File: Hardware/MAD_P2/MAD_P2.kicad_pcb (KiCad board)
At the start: 4 copper layers, 132.1 x 145.5 mm, 305 parts, among them J1 Line_3, J10 Conn_02x05_Odd_Even, J11 Conn_02x05_Odd_Even, J12 Micro_SD_Card, J13 Conn_02x05_Odd_Even, J14 Conn_02x05_Odd_Even, J15 Conn_ADC1, J16 Conn_DAC, J17 Conn_ADC2, J18 P3, J19 P4, J2 Line_1, J20 P2, J21 Conn_02x05_Odd_Even, J22 Conn_02x05_Odd_Even, J23 Conn_02x03_Odd_Even, J24 P5, J25 P6, J26 P7, J3 Line_2, J4 Power_In, J5 Micro_SD_Card, J6 Edge_Conn, J7 Conn_02x05_Odd_Even, J8 USB_C_Receptacle_USB2.0, J9 Conn_02x05_Odd_Even, P10 CONN_01X01, P11 CONN_01X01, P13 CONN_01X01, P8 CONN_01X01, Q1 MMBT3904, U1 P2X8C4M64P-REF, U10 AMS1117-3.3, U11 APM4953, U12 APM4953, U13 XL1509-5.0, U14 XL1509-5.0, U15 AMS1117-3.3, U16 AMS1117-3.3, U17 AMS1117-3.3, U18 AMS1117-3.3, U19 AMS1117-1.8, U2 XL1509-5.0, U20 LM321, U21 APM4953, U22 XL1509-5.0, U23 AMS1117-3.3, U24 AMS1117-3.3, U25 AMS1117-1.8, U26 W25Q128JVS, U27 FT232RL, U28 DS3231M, U29 ESP-12F, U3 XL1509-5.0, U30 ADS131E08-REF, U31 MAX5134-7, U4 XL1509-5.0, U5 XL1509-5.0, U6 AMS1117-3.3, U7 AMS1117-3.3, U8 AMS1117-3.3, U9 AMS1117-3.3, Y1 20MHz

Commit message: revising pcb layout
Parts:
- removed C132, C133, C134: 470pF, Capacitor_SMD:C_0603_1608Metric
- removed C135: 47pF, Capacitor_SMD:C_0603_1608Metric
- removed C136, C138: 0.1uF, Capacitor_SMD:C_0603_1608Metric
- removed C137, C139: 4.7uF, Capacitor_SMD:C_0603_1608Metric
- removed TP14: ADC_AMPP, TestPoint:TestPoint_Pad_1.0x1.0mm
- removed TP15: ADC_AMPN, TestPoint:TestPoint_Pad_1.0x1.0mm
- removed TP16: ADC_AMPOUT, TestPoint:TestPoint_Pad_1.0x1.0mm
- removed U25: AMS1117-1.8, Package_TO_SOT_SMD:SOT-223-3_TabPin2
- removed U30: ADS131E08-REF, Package_QFP:TQFP-64_10x10mm_P0.5mm
- removed U31: MAX5134-7, Package_SO:TSSOP-16_4.4x5mm_P0.65mm
- added D13: BLUE, LED_SMD:LED_0603_1608Metric, F.Cu at (324.0, 62.8)
- added D14: BLUE, LED_SMD:LED_0603_1608Metric, F.Cu at (314.7, 69.9)
- added D15: BLUE, LED_SMD:LED_0603_1608Metric, F.Cu at (357.2, 29.0)
- added D16: BLUE, LED_SMD:LED_0603_1608Metric, F.Cu at (357.2, 31.6)
- added D17: BLUE, LED_SMD:LED_0603_1608Metric, F.Cu at (318.7, 69.9)
- added D18: BLUE, LED_SMD:LED_0603_1608Metric, F.Cu at (341.9, 49.5)
- added D19: BLUE, LED_SMD:LED_0603_1608Metric, F.Cu at (328.0, 62.8)
- added D20: BLUE, LED_SMD:LED_0603_1608Metric, F.Cu at (324.0, 68.0)
- added D21: BLUE, LED_SMD:LED_0603_1608Metric, F.Cu at (324.0, 65.4)
- added D22: BLUE, LED_SMD:LED_0603_1608Metric, F.Cu at (346.2, 45.9)
- added D5: BLUE, LED_SMD:LED_0603_1608Metric, F.Cu at (357.2, 34.2)
- added D7: BLUE, LED_SMD:LED_0603_1608Metric, F.Cu at (306.6, 69.9)
- added D8: BLUE, LED_SMD:LED_0603_1608Metric, F.Cu at (310.6, 69.9)
- added F1: 5A, Fuse:Fuse_1206_3216Metric, F.Cu at (402.4, 19.9)
- added F2: 5A, Fuse:Fuse_1206_3216Metric, F.Cu at (410.8, 19.7)
- added F3: 5A, Fuse:Fuse_1206_3216Metric, F.Cu at (413.3, 19.8)
- added F5: 5A, Fuse:Fuse_1206_3216Metric, F.Cu at (421.7, 19.9)
- added J27: Line_1_1, MAD_P2:0705530001, B.Cu at (418.6, 27.3)
- added J28: Line_2_1, MAD_P2:0705530001, B.Cu at (445.4, 27.3)
- added J29: Line_2_3, MAD_P2:0705530001, B.Cu at (463.3, 27.3)
- added J30: Line_3_2, MAD_P2:0705530001, B.Cu at (481.2, 27.3)
- added J31: Micro_SD_Card_Connector, Tensile_Board:WM26501, F.Cu at (372.0, 30.8)
- added J32: Micro_SD_Card_Socket, Connector_Card:microSD_HC_Hirose_DM3D-SF, B.Cu at (372.0, 38.5)
- added J33: Shifted IO, Connector_PinSocket_2.54mm:PinSocket_1x06_P2.54mm_Vertical, F.Cu at (280.7, 78.5)
- added JP11: Jumper_1_3.3V, Jumper:SolderJumper-2_P1.3mm_Open_Pad1.0x1.5mm, F.Cu at (342.0, 46.4)
- added JP12: Jumper_1_5V, Jumper:SolderJumper-2_P1.3mm_Open_Pad1.0x1.5mm, F.Cu at (302.3, 70.4)
- added JP22: Jumper_1_3.3V, Jumper:SolderJumper-2_P1.3mm_Open_Pad1.0x1.5mm, F.Cu at (284.9, 70.4)
- added JP23: Jumper_1_5V, Jumper:SolderJumper-2_P1.3mm_Open_Pad1.0x1.5mm, F.Cu at (280.6, 66.8)
- added JP24: Jumper_1_VIN, Jumper:SolderJumper-2_P1.3mm_Open_Pad1.0x1.5mm, F.Cu at (302.3, 66.8)
- added JP25: Jumper_2_3.3V, Jumper:SolderJumper-2_P1.3mm_Open_Pad1.0x1.5mm, F.Cu at (306.7, 63.3)
- added JP26: Jumper_2_5V, Jumper:SolderJumper-2_P1.3mm_Open_Pad1.0x1.5mm, F.Cu at (302.3, 63.3)
- added JP27: Jumper_2_VIN, Jumper:SolderJumper-2_P1.3mm_Open_Pad1.0x1.5mm, F.Cu at (284.9, 63.3)
- added JP28: Jumper_2_3.3V, Jumper:SolderJumper-2_P1.3mm_Open_Pad1.0x1.5mm, F.Cu at (280.6, 63.3)
- added JP29: Jumper_2_5V, Jumper:SolderJumper-2_P1.3mm_Open_Pad1.0x1.5mm, F.Cu at (289.3, 63.3)
- added JP30: Jumper_2_VIN, Jumper:SolderJumper-2_P1.3mm_Open_Pad1.0x1.5mm, F.Cu at (293.6, 63.3)
- added JP31: Jumper_3_3.3V, Jumper:SolderJumper-2_P1.3mm_Open_Pad1.0x1.5mm, F.Cu at (289.3, 66.8)
- added JP32: Jumper_3_5V, Jumper:SolderJumper-2_P1.3mm_Open_Pad1.0x1.5mm, F.Cu at (280.6, 70.4)
- added JP33: Jumper_3_VIN, Jumper:SolderJumper-2_P1.3mm_Open_Pad1.0x1.5mm, F.Cu at (298.0, 63.3)
- added JP34: Jumper_1_3.3V, Jumper:SolderJumper-2_P1.3mm_Open_Pad1.0x1.5mm, F.Cu at (289.3, 70.4)
- added JP35: Jumper_1_5V, Jumper:SolderJumper-2_P1.3mm_Open_Pad1.0x1.5mm, F.Cu at (293.6, 66.8)
- added JP36: Jumper_1_VIN, Jumper:SolderJumper-2_P1.3mm_Open_Pad1.0x1.5mm, F.Cu at (293.6, 70.4)
- added JP37: ADC_32, Jumper:SolderJumper-2_P1.3mm_Open_Pad1.0x1.5mm, F.Cu at (289.3, 96.5)
- added JP38: ADC_SYNM, Jumper:SolderJumper-2_P1.3mm_Open_Pad1.0x1.5mm, F.Cu at (308.7, 78.0)
- added JP39: ADC_CS, Jumper:SolderJumper-2_P1.3mm_Open_Pad1.0x1.5mm, F.Cu at (293.8, 94.9)
- added JP40: ADC_SE, Jumper:SolderJumper-2_P1.3mm_Open_Pad1.0x1.5mm, F.Cu at (303.4, 83.9)
- added JP41: ADC_SE, Jumper:SolderJumper-2_P1.3mm_Open_Pad1.0x1.5mm, F.Cu at (298.5, 89.8)
- added JP42: ADC_SE, Jumper:SolderJumper-2_P1.3mm_Open_Pad1.0x1.5mm, F.Cu at (308.7, 81.5)
- added JP43: ADC_SE, Jumper:SolderJumper-2_P1.3mm_Open_Pad1.0x1.5mm, F.Cu at (289.3, 100.0)
- added Q2: 2N7002, Package_TO_SOT_SMD:SOT-23, F.Cu at (289.4, 92.4)
- added Q3: 2N7002, Package_TO_SOT_SMD:SOT-23, F.Cu at (285.2, 87.9)
- added Q4: 2N7002, Package_TO_SOT_SMD:SOT-23, F.Cu at (294.1, 87.9)
- added Q5: 2N7002, Package_TO_SOT_SMD:SOT-23, F.Cu at (289.7, 87.9)
- added R12: 620R, Resistor_SMD:R_0603_1608Metric, F.Cu at (345.9, 49.4)
- added R13: 620R, Resistor_SMD:R_0603_1608Metric, F.Cu at (341.8, 52.0)
- added R3: 620R, Resistor_SMD:R_0603_1608Metric, F.Cu at (328.0, 67.9)
- added R4: 1K, Resistor_SMD:R_0603_1608Metric, F.Cu at (350.2, 45.9)
- added R5: 620R, Resistor_SMD:R_0603_1608Metric, F.Cu at (332.0, 62.8)
- added R55: 100R, Resistor_SMD:R_0603_1608Metric, F.Cu at (305.6, 97.8)
- added R56: 100R, Resistor_SMD:R_0603_1608Metric, F.Cu at (310.7, 92.5)
- added R57: X, Resistor_SMD:R_0805_2012Metric, F.Cu at (299.0, 83.6)
- added R58: X, Resistor_SMD:R_0805_2012Metric, F.Cu at (294.6, 82.1)
- added R59: X, Resistor_SMD:R_0805_2012Metric, F.Cu at (299.9, 80.6)
- added R60: X, Resistor_SMD:R_0805_2012Metric, F.Cu at (304.3, 77.7)
- added R61: 10K, Resistor_SMD:R_0603_1608Metric, F.Cu at (320.9, 82.5)
- added R62: X, Resistor_SMD:R_0805_2012Metric, F.Cu at (304.3, 80.6)
- added R63: X, Resistor_SMD:R_0805_2012Metric, F.Cu at (293.8, 91.6)
- added R64: X, Resistor_SMD:R_0805_2012Metric, F.Cu at (299.9, 77.7)
- added R65: X, Resistor_SMD:R_0805_2012Metric, F.Cu at (298.6, 86.5)
- added R7: 1K, Resistor_SMD:R_0603_1608Metric, F.Cu at (322.7, 70.5)
- added R8: 1K, Resistor_SMD:R_0603_1608Metric, F.Cu at (357.2, 36.7)
- added SW1: Switch_SW_Push, Button_Switch_THT:SW_PUSH_6mm, F.Cu at (330.2, 78.2)
- added Y2: 16.384MHz, Crystal:Crystal_SMD_3225-4Pin_3.2x2.5mm, F.Cu at (295.1, 78.4)
- C102, C86, C96: value 1uF -> 4.7uF
- C108: value 1uF -> 270nF
- C109, C111: value 0.1uF -> 1uF
- C113: value 1uF -> 8.2pF
- C114: value 0.1uF -> 8.2pF
- C115: value 22uF -> 1uF
- C116: value 1uF -> 2.7nF
- C117: value 0.1uF -> 2.7nF
- C118: value 10uF -> 2.7nF
- C119, C122, C123, C125, C126, C128, C129, C131: value 470pF -> 100pF
- C120: value 470pF -> 2.7nF
- C121, C124, C127, C130: value 470pF -> 1nF
- C82: value 4.7uF -> 1uF
- C94: value 4.7uF -> 47pF
- C98: value 1uF -> 0.1uF
- C99: value 4.7uF -> 0.1uF
- J1: value Line_3 -> Line_1_3; footprint Connector_AMASS:AMASS_XT30PW-M_1x02_P2.50mm_Horizontal -> MAD_P2:0705530001; moved to B.Cu
- J12: value Micro_SD_Card -> Line_3_3; footprint Tensile_Board:WM26501 -> MAD_P2:0705530001; moved to B.Cu
- J17: value Conn_ADC2 -> Line_1_2; footprint Connector_IDC:IDC-Header_2x05_P2.54mm_Vertical -> MAD_P2:0705530001
- J2: value Line_1 -> Line_2_2; footprint Connector_AMASS:AMASS_XT30PW-M_1x02_P2.50mm_Horizontal -> MAD_P2:0705530001; moved to B.Cu
- J3: value Line_2 -> Line_3_1; footprint Connector_AMASS:AMASS_XT30PW-M_1x02_P2.50mm_Horizontal -> MAD_P2:0705530001; moved to B.Cu
- J4: footprint Connector_AMASS:AMASS_XT30PW-M_1x02_P2.50mm_Horizontal -> MAD_P2:0705530001; moved to B.Cu
- JP1: value Jumper_3_3.3V -> Jumper_2_3.3V; footprint Connector_PinHeader_2.54mm:PinHeader_1x02_P2.54mm_Vertical -> Jumper:SolderJumper-2_P1.3mm_Open_Pad1.0x1.5mm
- JP2: value Jumper_3_5V -> Jumper_2_5V; footprint Connector_PinHeader_2.54mm:PinHeader_1x02_P2.54mm_Vertical -> Jumper:SolderJumper-2_P1.3mm_Open_Pad1.0x1.5mm
- JP21: value ADC_CS -> Jumper_1_VIN
- JP3: value Jumper_3_VIN -> Jumper_2_VIN; footprint Connector_PinHeader_2.54mm:PinHeader_1x02_P2.54mm_Vertical -> Jumper:SolderJumper-2_P1.3mm_Open_Pad1.0x1.5mm
- JP4: value Jumper_2_3.3V -> Jumper_3_3.3V; footprint Connector_PinHeader_2.54mm:PinHeader_1x02_P2.54mm_Vertical -> Jumper:SolderJumper-2_P1.3mm_Open_Pad1.0x1.5mm
- JP5: value Jumper_2_5V -> Jumper_3_5V; footprint Connector_PinHeader_2.54mm:PinHeader_1x02_P2.54mm_Vertical -> Jumper:SolderJumper-2_P1.3mm_Open_Pad1.0x1.5mm
- JP6: value Jumper_2_VIN -> Jumper_3_VIN; footprint Connector_PinHeader_2.54mm:PinHeader_1x02_P2.54mm_Vertical -> Jumper:SolderJumper-2_P1.3mm_Open_Pad1.0x1.5mm
- JP7: value Jumper_1_3.3V -> Jumper_3_3.3V; footprint Connector_PinHeader_2.54mm:PinHeader_1x02_P2.54mm_Vertical -> Jumper:SolderJumper-2_P1.3mm_Open_Pad1.0x1.5mm
- JP8: value Jumper_1_5V -> Jumper_3_5V; footprint Connector_PinHeader_2.54mm:PinHeader_1x02_P2.54mm_Vertical -> Jumper:SolderJumper-2_P1.3mm_Open_Pad1.0x1.5mm
- JP9: value Jumper_1_VIN -> Jumper_3_VIN; footprint Connector_PinHeader_2.54mm:PinHeader_1x02_P2.54mm_Vertical -> Jumper:SolderJumper-2_P1.3mm_Open_Pad1.0x1.5mm
- R18, R19: value 1K -> 240R
- R25: value 240R -> 1K
- R30: value X -> 620R
- R31, R33, R34: value 10K -> 1K
- R32: value 10K -> 620R
- R35, R36: value 10K -> 240R
- R39, R40, R51, R52, R53, R54: value 10K -> 100R
- R44: value 10K -> 1M
- U17: value AMS1117-3.3 -> MAX5134-7; footprint Package_TO_SOT_SMD:SOT-223-3_TabPin2 -> Package_SO:TSSOP-16_4.4x5mm_P0.65mm
- U23: value AMS1117-3.3 -> ADS131A04; footprint Package_TO_SOT_SMD:SOT-223-3_TabPin2 -> Package_QFP:LQFP-32_5x5mm_P0.5mm
- moved R44 291.9 mm to (297.5, 100.4), turned to 0 degrees
- moved JP21 289.4 mm to (298.0, 70.4)
- moved R37 289.2 mm to (301.5, 97.8), turned to 0 degrees
- moved C113 286.9 mm to (302.8, 86.9), turned to 0 degrees
- moved C119 286.5 mm to (314.0, 95.0), turned to 0 degrees
- moved R43 286.1 mm to (305.6, 100.3), turned to 0 degrees
- moved R45 286.0 mm to (301.5, 100.3), turned to 0 degrees
- moved C126 284.4 mm to (302.0, 95.3), turned to 0 degrees
- moved C118 283.6 mm to (309.6, 100.0), turned to 0 degrees
- moved R42 282.5 mm to (310.0, 95.0), turned to 0 degrees
- moved C108 280.7 mm to (307.6, 84.6), turned to 0 degrees
- moved C130 280.1 mm to (293.5, 97.9), turned to 0 degrees
- moved R25 279.7 mm to (341.8, 54.5), turned to 0 degrees
- moved C123 277.1 mm to (312.9, 82.5), turned to 0 degrees
- moved C117 276.9 mm to (313.6, 97.5), turned to 0 degrees
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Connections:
- C102 pad 1: 1.8V_ADC -> 3.3V_ADC
- C108 pad 1: GND -> Net-(C108-Pad1)
- C108 pad 2: Net-(C108-Pad2) -> GND
- C109 pad 1: 1.8V_ADC -> Net-(C109-Pad1)
- C110 pad 1: GND -> Net-(C110-Pad1)
- C110 pad 2: Net-(C110-Pad2) -> GND
- C111 pad 1: GND -> Net-(C111-Pad1)
- C111 pad 2: Net-(C110-Pad2) -> GND
- C112 pad 1: 1.8V_ADC -> 3.3V_ADC
- C114 pad 1: 3.3V_ADC -> GND
- C114 pad 2: GND -> Net-(C114-Pad2)
- C115 pad 1: GND -> 3.3V_ADC
- C115 pad 2: Net-(C115-Pad2) -> GND
- C116 pad 1: 3.3V_ADC -> /Peripherals/AIN2P
- C116 pad 2: GND -> /Peripherals/AIN2N
- C117 pad 1: GND -> /Peripherals/AIN3P
- C117 pad 2: Net-(C117-Pad2) -> /Peripherals/AIN3N
- C118 pad 1: GND -> /Peripherals/AIN4P
- C118 pad 2: Net-(C117-Pad2) -> /Peripherals/AIN4N
- C119 pad 2: /Peripherals/IN1P -> A1+
- C120 pad 1: /Peripherals/IN1N -> /Peripherals/AIN1P
- C120 pad 2: GND -> /Peripherals/AIN1N
- C121 pad 1: GND -> A1+
- C121 pad 2: /Peripherals/IN2P -> A1-
- C122 pad 1: /Peripherals/IN2N -> A1-
- C123 pad 2: /Peripherals/IN3P -> A2+
- C124 pad 1: /Peripherals/IN3N -> A2+
- C124 pad 2: GND -> A2-
- C125 pad 1: GND -> A2-
- C125 pad 2: /Peripherals/IN4P -> GND
- C126 pad 1: /Peripherals/IN4N -> GND
- C126 pad 2: GND -> A3+
- C127 pad 1: GND -> A3+
- C127 pad 2: /Peripherals/IN5P -> A3-
- C128 pad 1: /Peripherals/IN5N -> A3-
- C129 pad 2: /Peripherals/IN6P -> A4+
- C130 pad 1: /Peripherals/IN6N -> A4+
- C130 pad 2: GND -> A4-
- C131 pad 1: GND -> A4-
- C131 pad 2: /Peripherals/IN7P -> GND
- C73 pad 1: VIN_RAW -> Net-(C73-Pad1)
- C74 pad 1: VIN_RAW -> Net-(C74-Pad1)
- C75 pad 1: VIN_RAW -> Net-(C75-Pad1)
- C77 pad 1: VIN_IO -> VIN_L1
- C79 pad 1: Net-(C79-Pad1) -> 5V_MAIN1
- C82 pad 1: Net-(C79-Pad1) -> 3.3V_MAIN1
- C83 pad 1: Net-(C79-Pad1) -> 5V_MAIN1
- C86 pad 1: Net-(C79-Pad1) -> 3.3V_MAIN1
- C87 pad 1: Net-(C79-Pad1) -> 5V_MAIN1
- C91 pad 1: VIN_RAW -> Net-(C91-Pad1)
- C94 pad 1: 5V_ADC -> Net-(C94-Pad1)
- C96 pad 1: 5V_ADC -> 3.3V_ADC
- C98 pad 1: Net-(C98-Pad1) -> 3.3V_ADC
- C99 pad 1: Net-(C98-Pad1) -> 3.3V_ADC
- J11 pad 7: GND -> 3.3V_MAIN1
- J11 pad 8: GND -> 5V_MAIN1
- J12 pad 2: /Peripherals/P42 -> GND
- J17 pad 1: A5+ -> Net-(J17-Pad1)
- J17 pad 2: A5- -> GND
- J20 pad 2: 3.3V_MAIN -> 3.3V_MAIN1
- J20 pad 4: 3.3V_MAIN -> 3.3V_MAIN1
- J20 pad 5: 5V_MAIN -> 5V_MAIN1
- J23 pad 1: 5V_MAIN -> 5V_MAIN1
- JP1 pad 1: +3.3V_3 -> +3.3V_2
- JP1 pad 2: Net-(J1-Pad1) -> Net-(J2-Pad1)
- JP2 pad 1: +5V_3 -> +5V_2
- JP2 pad 2: Net-(J1-Pad1) -> Net-(J2-Pad1)
- JP21 pad 1: Net-(JP21-Pad1) -> VIN
- JP21 pad 2: /Peripherals/P47 -> Net-(J1-Pad1)
- JP3 pad 2: Net-(J1-Pad1) -> Net-(J2-Pad1)
- JP4 pad 1: +3.3V_2 -> +3.3V_3
- JP5 pad 1: +5V_2 -> +5V_3
- JP7 pad 1: +3.3V_1 -> +3.3V_3
- JP7 pad 2: Net-(J2-Pad1) -> Net-(J12-Pad1)
- JP8 pad 1: +5V_1 -> +5V_3
- JP8 pad 2: Net-(J2-Pad1) -> Net-(J12-Pad1)
- JP9 pad 2: Net-(J2-Pad1) -> Net-(J12-Pad1)
- L11 pad 2: Net-(C79-Pad1) -> 5V_MAIN1
- R1 pad 1: 5V_MAIN -> 5V_MAIN1
- R25 pad 1: /Peripherals/P39 -> +5V_1
- R25 pad 2: Net-(J12-Pad7) -> Net-(D17-Pad2)
- R30 pad 1: Net-(R30-Pad1) -> +3.3V_2
- R31 pad 1: Net-(R31-Pad1) -> +5V_2
- R31 pad 2: GND -> Net-(D19-Pad2)
- R32 pad 1: Net-(R32-Pad1) -> +3.3V_2
- R32 pad 2: GND -> Net-(D20-Pad2)
- R33 pad 1: 1.8V_ADC -> +5V_2
- R34 pad 1: Net-(R34-Pad1) -> /Power2/P55
- R34 pad 2: 1.8V_ADC -> Net-(D22-Pad2)
- R35 pad 1: Net-(R35-Pad1) -> /Connections/P39
- R35 pad 2: GND -> Net-(J31-Pad7)
- R36 pad 1: GND -> /Connections/P39
- R36 pad 2: Net-(JP21-Pad1) -> Net-(J32-Pad7)
- R37 pad 1: Net-(R37-Pad1) -> Net-(JP37-Pad2)
- R37 pad 2: 1.8V_ADC -> 3.3V_ADC
- R38 pad 1: Net-(R38-Pad1) -> +3V3
- R38 pad 2: GND -> /Peripherals/P51
- R39 pad 1: A1+ -> Net-(R39-Pad1)
- R39 pad 2: /Peripherals/IN1P -> /Peripherals/AIN1P
- R40 pad 2: /Peripherals/IN1N -> /Peripherals/AIN1N
- R41 pad 1: A2+ -> HS_VIN
- R41 pad 2: /Peripherals/IN2P -> HS_1
- R42 pad 1: A2- -> Net-(JP38-Pad2)
- R42 pad 2: /Peripherals/IN2N -> GND
- R43 pad 1: A3+ -> +3V3
- R43 pad 2: /Peripherals/IN3P -> /Peripherals/P52
- R44 pad 1: A3- -> Net-(C114-Pad2)
- R44 pad 2: /Peripherals/IN3N -> Net-(C113-Pad2)
- R45 pad 1: A4+ -> HS_VIN
- R45 pad 2: /Peripherals/IN4P -> HS_2
- R46 pad 1: A4- -> Net-(R46-Pad1)
- R46 pad 2: /Peripherals/IN4N -> 3.3V_ADC
- R47 pad 1: A5+ -> GND
- R47 pad 2: /Peripherals/IN5P -> Net-(JP39-Pad1)
- R48 pad 1: A5- -> +3V3
- R48 pad 2: /Peripherals/IN5N -> /Peripherals/P53
- R49 pad 1: A6+ -> HS_VIN
- R49 pad 2: /Peripherals/IN6P -> HS_3
- R50 pad 1: A6- -> +3V3
- R50 pad 2: /Peripherals/IN6N -> /Peripherals/P54
- R51 pad 1: A7+ -> Net-(R51-Pad1)
- R51 pad 2: /Peripherals/IN7P -> /Peripherals/AIN2P
- R52 pad 1: A7- -> A2-
- R52 pad 2: /Peripherals/IN7N -> /Peripherals/AIN2N
- R53 pad 1: A8+ -> Net-(R53-Pad1)
- R53 pad 2: /Peripherals/IN8P -> /Peripherals/AIN3P
- R54 pad 1: A8- -> A3-
- R54 pad 2: /Peripherals/IN8N -> /Peripherals/AIN3N
- U11 pad 5: VIN_RAW -> Net-(C91-Pad1)
- U11 pad 6: VIN_RAW -> Net-(C91-Pad1)
- U11 pad 7: VIN_RAW -> Net-(C73-Pad1)
- U11 pad 8: VIN_RAW -> Net-(C73-Pad1)
- U12 pad 5: VIN_RAW -> Net-(C74-Pad1)
- U12 pad 6: VIN_RAW -> Net-(C74-Pad1)
- U12 pad 7: VIN_RAW -> Net-(C75-Pad1)
- U12 pad 8: VIN_RAW -> Net-(C75-Pad1)
- U14 pad 1: VIN_IO -> VIN_L1
- U14 pad 3: Net-(C79-Pad1) -> 5V_MAIN1
- U17 pad 1: GND -> Net-(C94-Pad1)
- U17 pad 2: /Power2/V_32_35 -> 5V_ADC
- U17 pad 3: Net-(C79-Pad1) -> Net-(U17-Pad3)
- U18 pad 2: /Power2/V_48_51 -> 3.3V_MAIN1
- U18 pad 3: Net-(C79-Pad1) -> 5V_MAIN1
- U23 pad 1: GND -> /Peripherals/AIN1N
- U23 pad 2: Net-(C98-Pad1) -> /Peripherals/AIN1P
- U23 pad 3: 5V_ADC -> /Peripherals/AIN2N

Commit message: finished power supply board layout
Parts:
- SW1: moved to B.Cu
- moved TP9 259.7 mm to (397.9, 123.8), turned to 90 degrees
- moved TP8 254.3 mm to (402.4, 123.8), turned to 90 degrees
- moved R28 251.2 mm to (406.5, 119.4), turned to 270 degrees
- moved JP19 249.1 mm to (406.5, 123.1), turned to 90 degrees
- moved JP18 248.7 mm to (398.0, 146.8), turned to 180 degrees
- moved R27 245.7 mm to (409.0, 123.3), turned to 90 degrees
- moved U29 244.8 mm to (404.6, 135.1), turned to 90 degrees
- moved R24 244.2 mm to (401.3, 147.0), turned to 270 degrees
- moved R26 243.1 mm to (411.0, 123.3), turned to 90 degrees
- moved TP1 241.8 mm to (403.2, 146.5), turned to 180 degrees
- moved R23 238.6 mm to (405.4, 147.1), turned to 270 degrees
- moved R29 237.9 mm to (415.2, 123.3), turned to 270 degrees
- moved TP13 234.6 mm to (408.3, 147.1), turned to 90 degrees
- moved TP12 230.3 mm to (411.5, 147.1), turned to 90 degrees
- moved TP7 227.9 mm to (420.2, 128.2), turned to 270 degrees
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
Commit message: begining layout of adc/dac
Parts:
- moved JP20 192.2 mm to (433.7, 151.8), turned to 270 degrees
- moved JP32 189.0 mm to (463.0, 20.6)
- moved JP9 186.4 mm to (487.5, 21.7)
- moved R58 183.5 mm to (470.3, 135.3), turned to 180 degrees
- moved JP8 182.0 mm to (487.7, 19.3)
- moved R63 181.2 mm to (470.3, 132.7)
- moved JP31 180.6 mm to (462.9, 17.2)
- moved JP41 179.6 mm to (469.9, 143.5)
- moved JP28 178.8 mm to (453.4, 17.4)
- moved JP7 178.4 mm to (487.7, 16.9)
- moved R57 170.7 mm to (461.3, 136.5), turned to 180 degrees
- moved C120 170.6 mm to (461.1, 141.6), turned to 180 degrees
- moved JP2 170.1 mm to (448.8, 21.2)
- moved JP33 169.6 mm to (462.8, 23.3)
- moved JP29 169.6 mm to (453.4, 20.4)
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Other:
- board size 132.1 x 145.5 mm -> 121.6 x 145.5 mm

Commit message: general layout complete
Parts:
- BT1: moved to F.Cu
- moved C82 181.5 mm to (502.0, 117.7), turned to 270 degrees
- moved C86 165.3 mm to (503.9, 117.7), turned to 270 degrees
- moved R1 146.4 mm to (436.7, 61.0), turned to 180 degrees
- moved R35 129.1 mm to (438.0, 145.9), turned to 270 degrees
- moved R36 127.7 mm to (440.1, 145.9), turned to 270 degrees
- moved D15 117.1 mm to (379.5, 144.0)
- moved R32 116.6 mm to (382.9, 153.0), turned to 180 degrees
- moved D16 116.3 mm to (379.5, 145.8)
- moved D22 115.6 mm to (379.5, 156.6)
- moved JP18 113.6 mm to (511.3, 155.2), turned to 270 degrees
- moved C94 111.9 mm to (460.4, 129.2)
- moved R33 111.3 mm to (382.9, 154.8), turned to 180 degrees
- moved R24 110.3 mm to (511.5, 151.9), turned to 0 degrees
- moved U17 108.9 mm to (454.4, 131.3)
- moved R8 108.5 mm to (382.9, 142.2), turned to 180 degrees
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
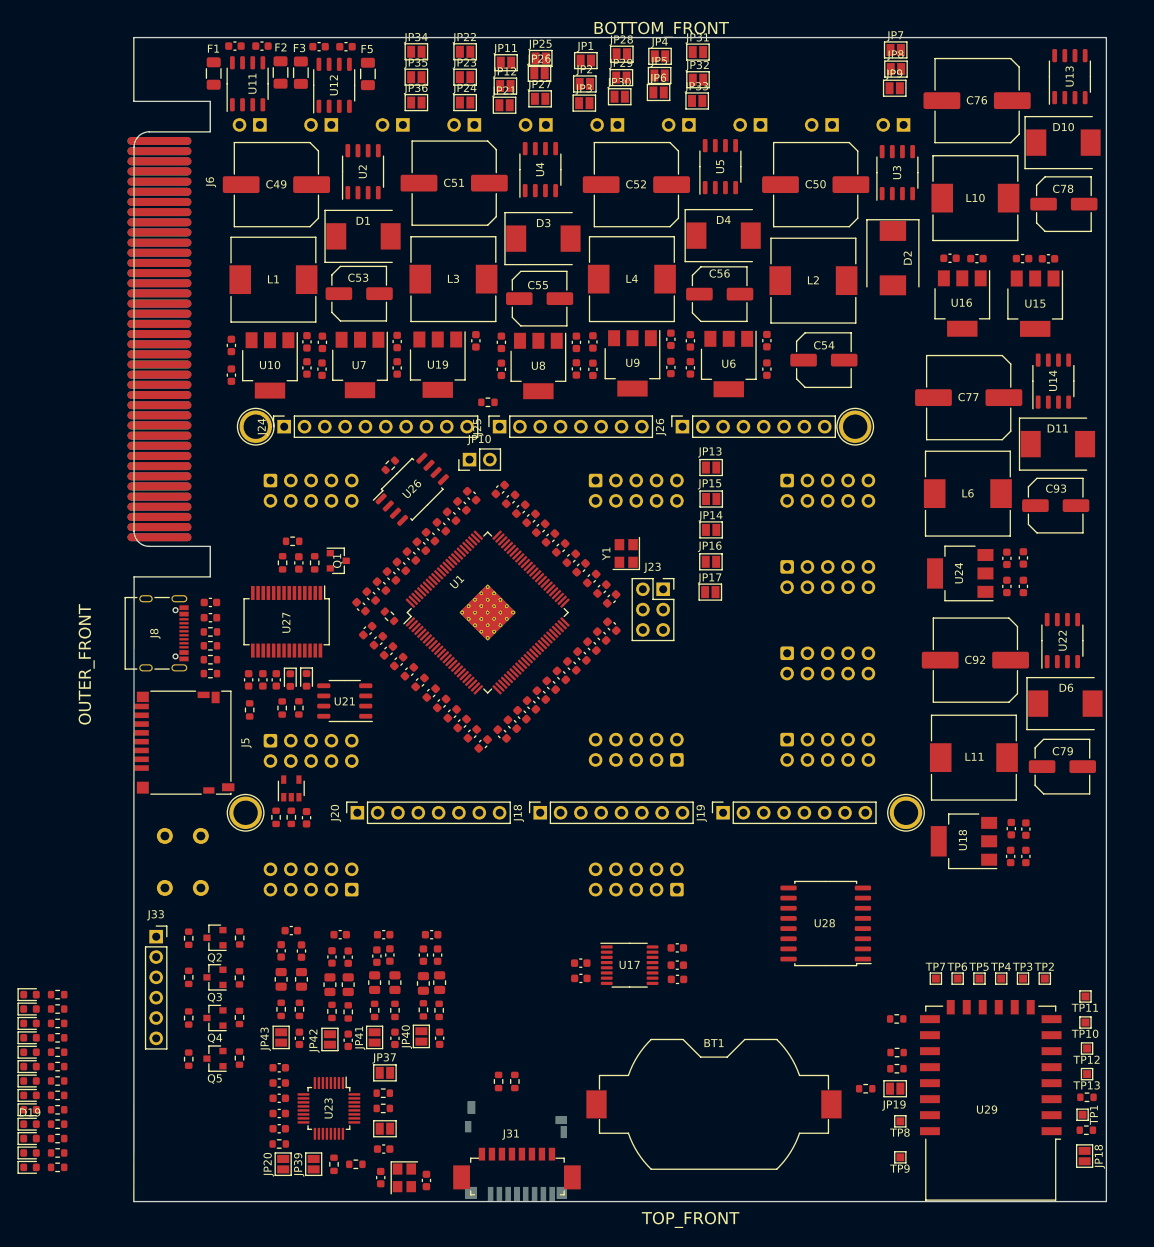
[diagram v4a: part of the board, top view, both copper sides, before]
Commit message: routing power section
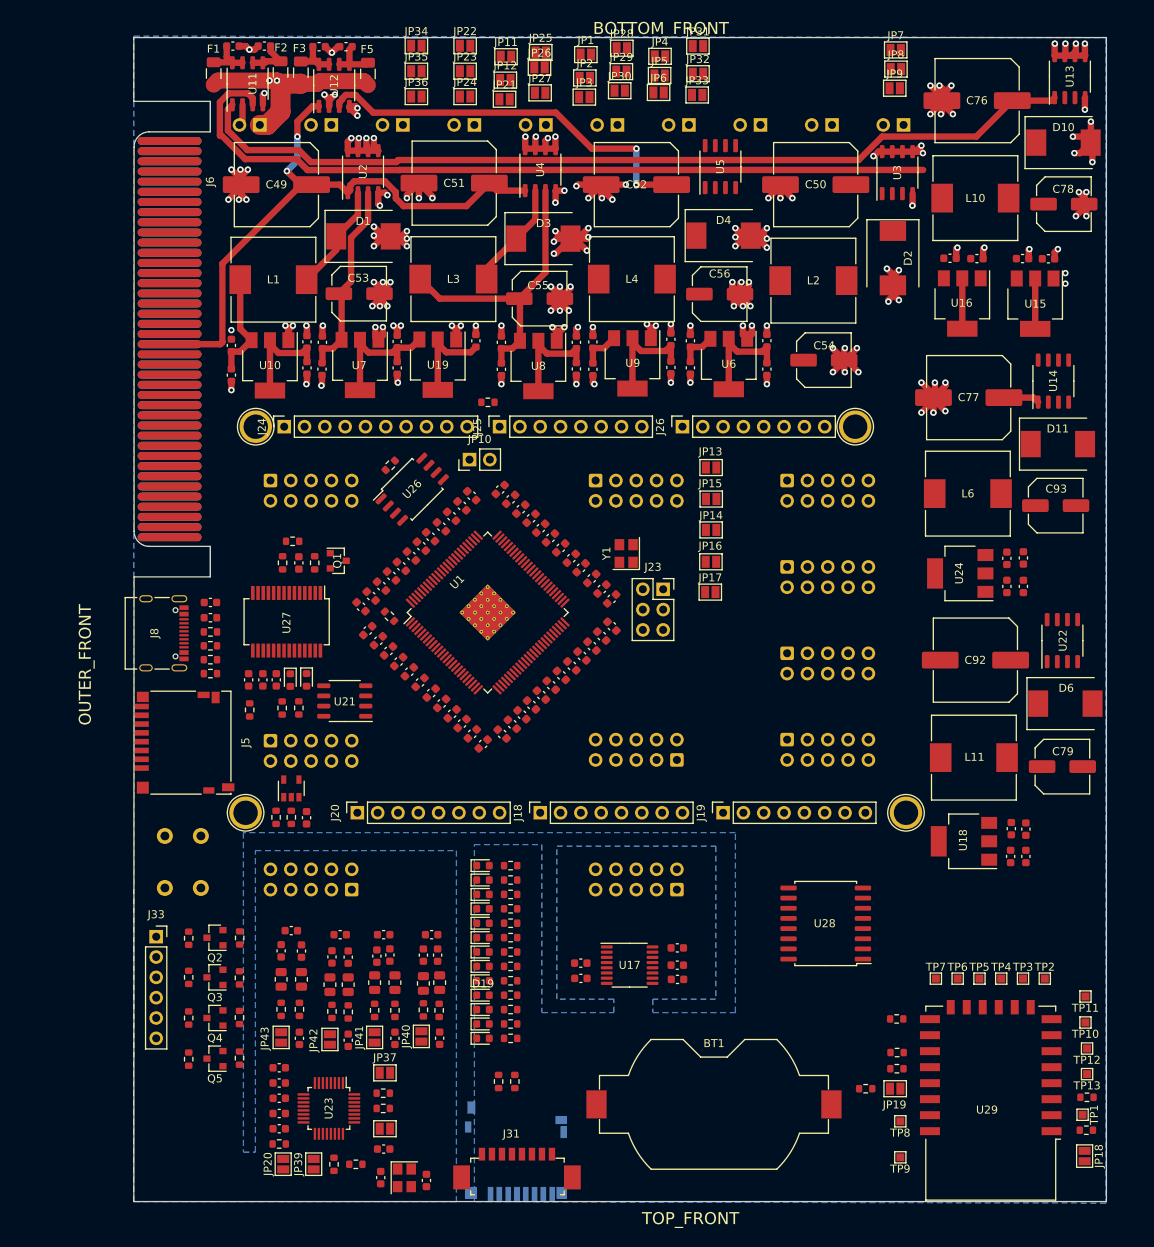
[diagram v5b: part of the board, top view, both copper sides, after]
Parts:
- moved D13 58.9 mm to (436.1, 124.3)
- moved D14 58.9 mm to (436.1, 126.1)
- moved D15 58.9 mm to (436.1, 127.9)
- moved D16 58.9 mm to (436.1, 129.7)
- moved D17 58.9 mm to (436.1, 131.5)
- moved D18 58.9 mm to (436.1, 133.3)
- moved D19 58.9 mm to (436.1, 135.1)
- moved D20 58.9 mm to (436.1, 136.9)
- moved D21 58.9 mm to (436.1, 138.7)
- moved D22 58.9 mm to (436.1, 140.5)
- moved D5 58.9 mm to (436.1, 118.9)
- moved D7 58.9 mm to (436.1, 120.7)
- moved D8 58.9 mm to (436.1, 122.5)
- moved R12 58.9 mm to (439.5, 127.9)
- moved R13 58.9 mm to (439.5, 129.7)
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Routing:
- net GND: track 0.00 -> 295.9 mm, vias 0 -> 151
- net VIN_IO: track 0.00 -> 111.8 mm
- net VIN_ADC: track 0.00 -> 99.5 mm
- net VIN_L1: track 0.00 -> 81.7 mm, vias 0 -> 2
- net VIN_L2: track 0.00 -> 49.8 mm, vias 0 -> 2
- net +5V: track 0.00 -> 38.2 mm
- net +5V_1: track 0.00 -> 38.1 mm
- net VIN_RAW: track 0.00 -> 27.1 mm, vias 0 -> 2
- net Net-(C70-Pad1): track 0.00 -> 17.1 mm
- net +3.3V_2: track 0.00 -> 14.3 mm
- net +3.3V_3: track 0.00 -> 14.3 mm
- net +3.3V_1: track 0.00 -> 14.1 mm
- net +3V3: track 0.00 -> 13.9 mm
- net Net-(D3-Pad1): track 0.00 -> 13.6 mm
- net Net-(D1-Pad1): track 0.00 -> 13.5 mm
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- added copper zone on B.Cu, net GND
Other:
- copper layers 4 -> 2
